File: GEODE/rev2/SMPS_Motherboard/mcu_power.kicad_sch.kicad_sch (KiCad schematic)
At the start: 32 parts, among them J402 Conn_Picoblade_JST_DEBUG, J403 USB4105-GF-A, U401 STM32G483RET6, Y401 ABM8W-48.0000MHZ-4-D1X-T3

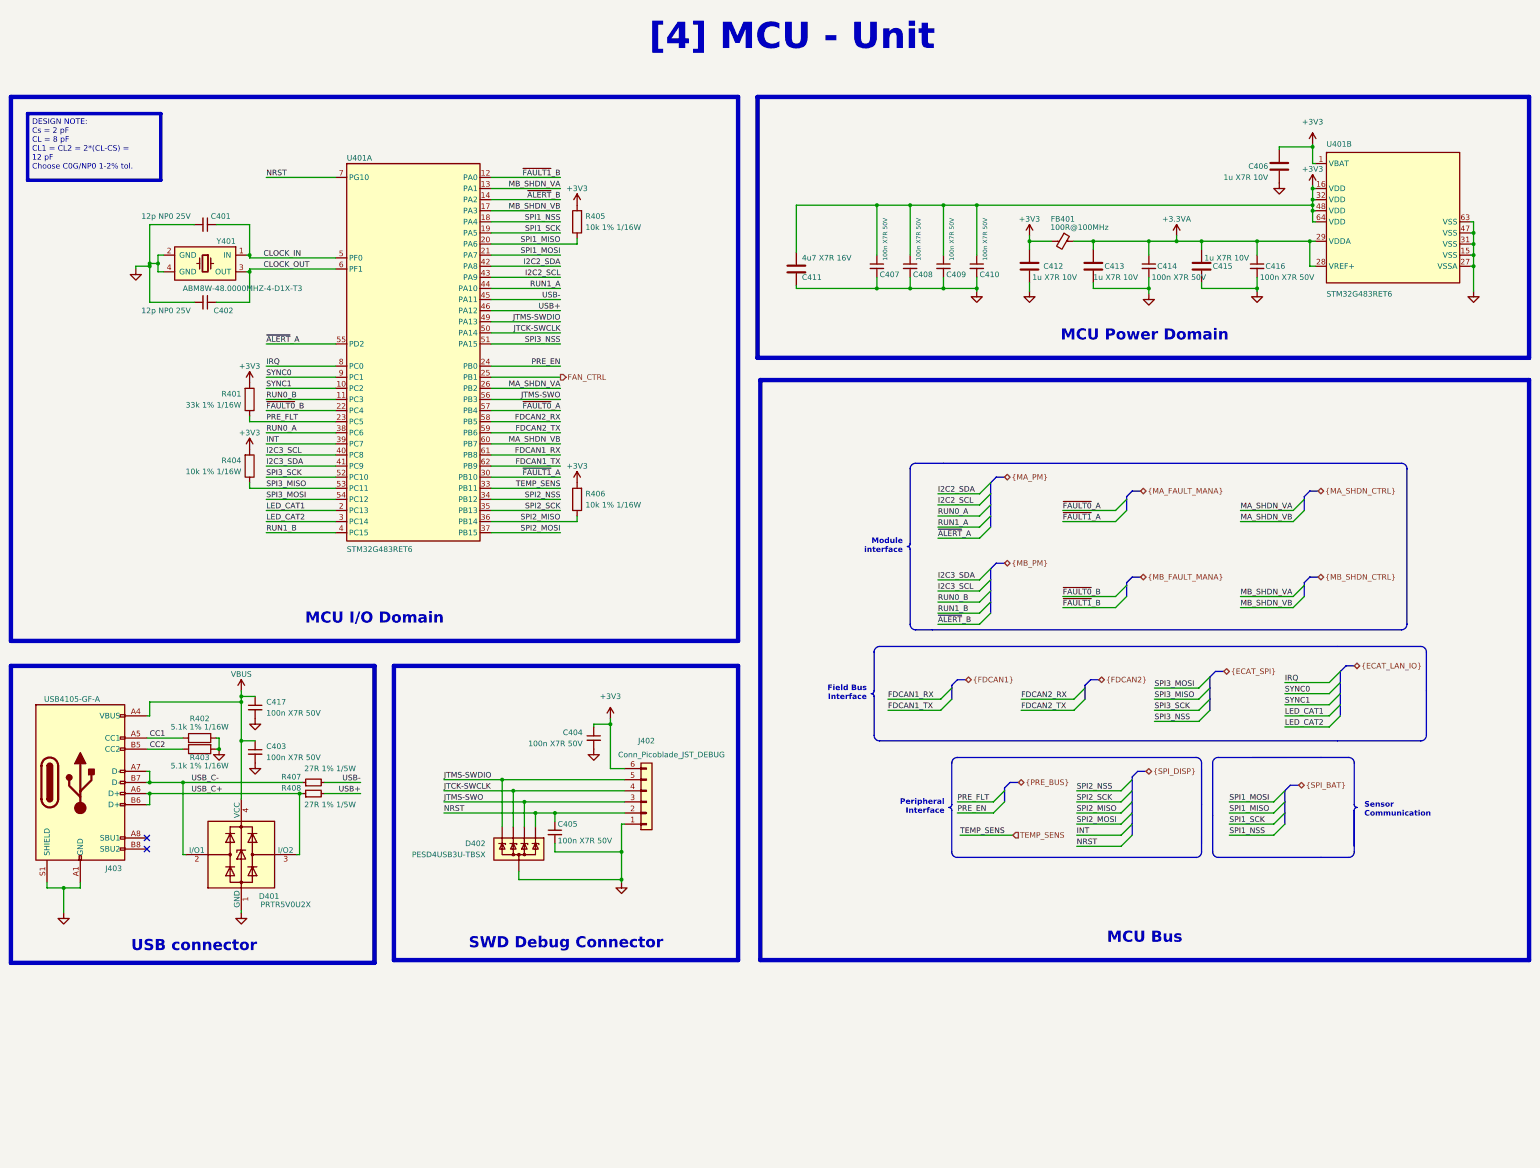
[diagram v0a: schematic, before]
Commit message: changed connectors, removed can, added fuse, disconnected EXTVCC in power generation
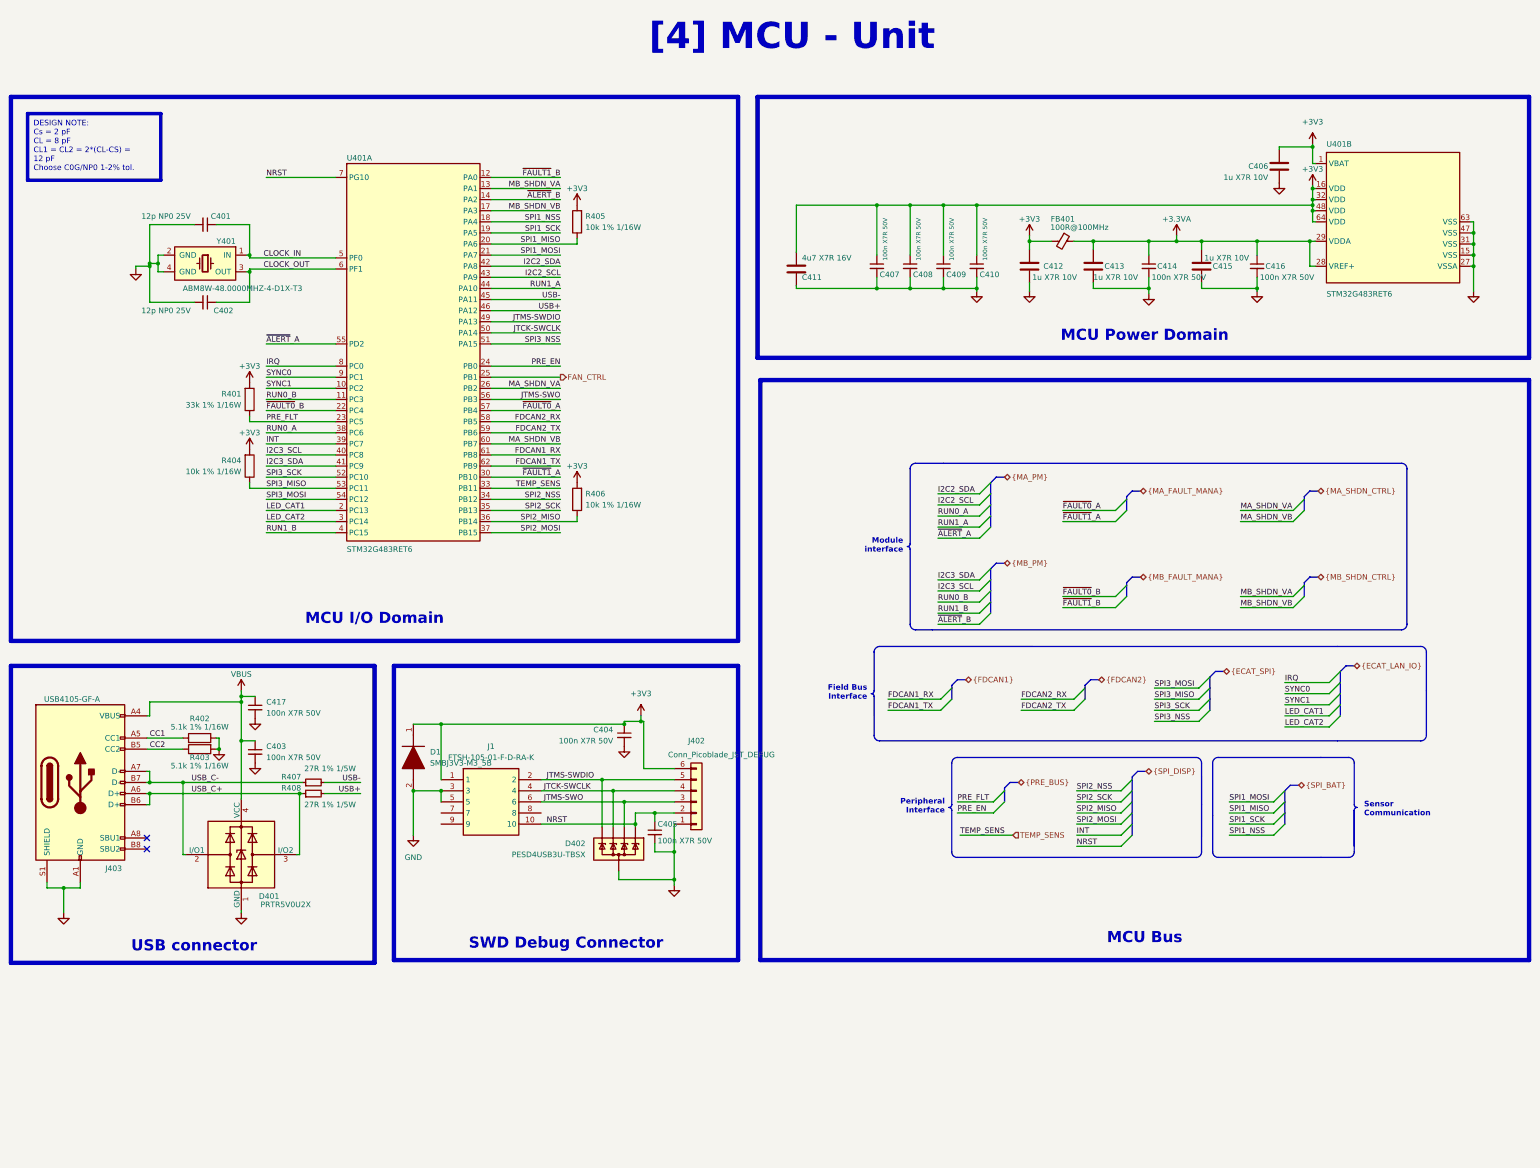
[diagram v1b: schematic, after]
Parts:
- added D1: SMBJ3V3-M3_5B, DIONM5436X244N, symbol SamacSys_Parts:SMBJ3V3-M3_5B
- added J1: FTSH-105-01-F-D-RA-K, FTSH-105-XX-YYY-D-RA-K, symbol SamacSys_Parts:FTSH-105-01-F-D-RA-K
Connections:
- net +3V3: now also D1.1 (K), J1.1
- net GND: now also D1.2 (A), J1.3, J1.5
- net JTCK-SWCLK: now also J1.4
- net JTMS-SWDIO: now also J1.2
- net JTMS-SWO: now also J1.6
- net NRST: now also J1.10
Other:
- moved on the sheet: C404, C405, D402, J402

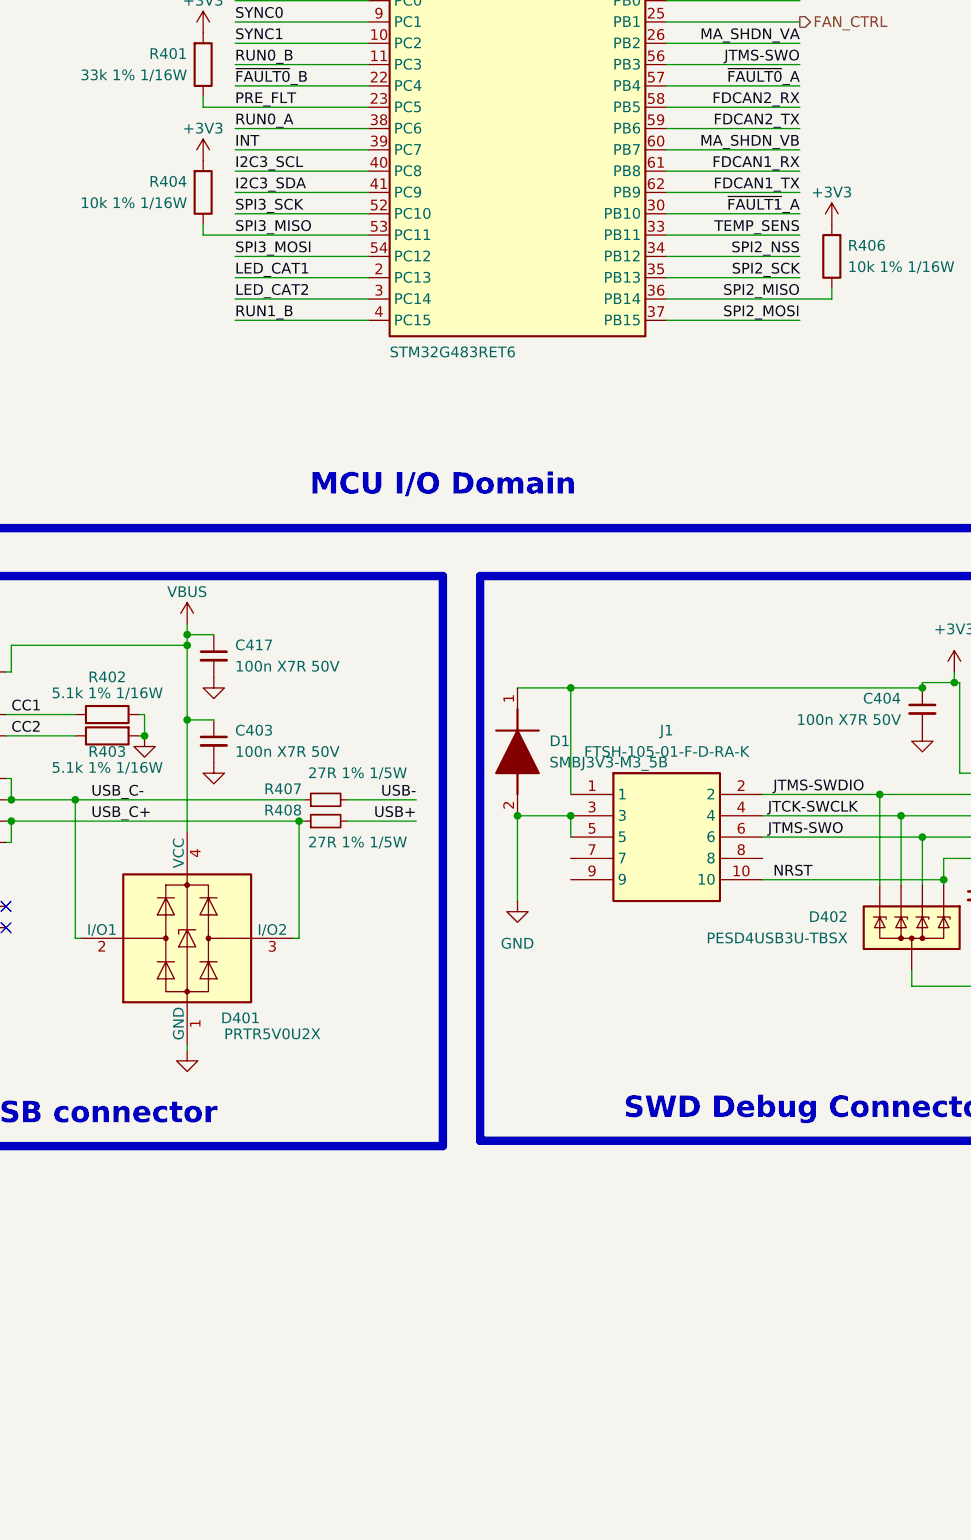
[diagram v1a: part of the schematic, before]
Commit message: replaced output connectors, added UART connector, removed fuse - schematics
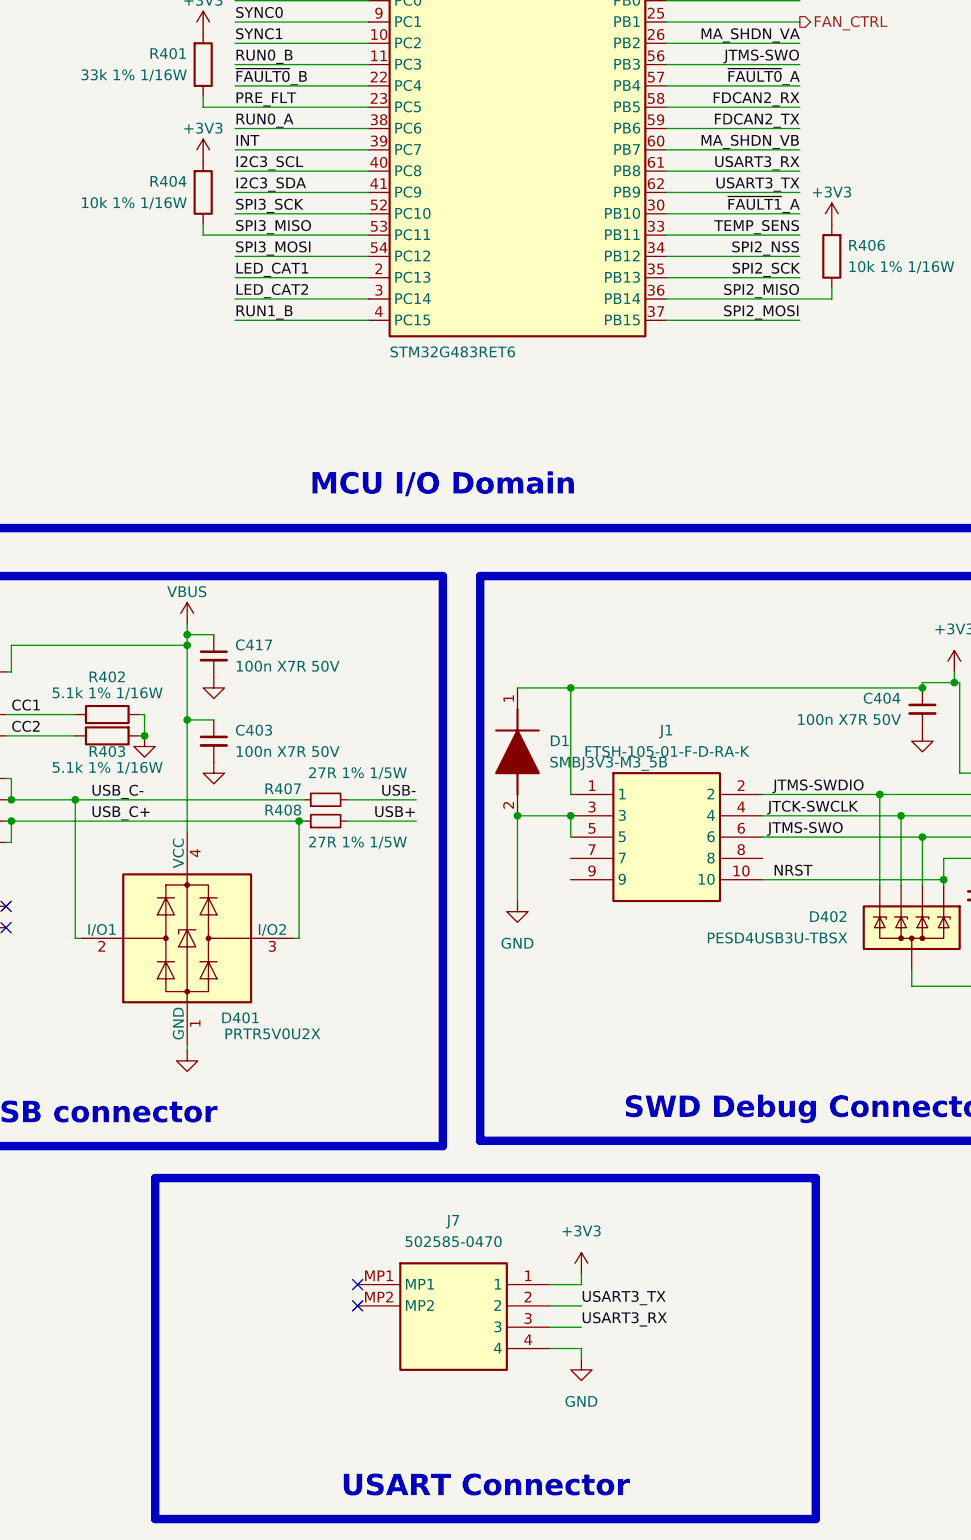
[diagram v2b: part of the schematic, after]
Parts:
- added J7: 502585-0470, 5025850470, symbol SamacSys_Parts:502585-0470
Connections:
- net +3V3: now also J7.1
- net FDCAN1_RX: no longer U401.61 (PB8)
- net FDCAN1_TX: no longer U401.62 (PB9)
- net GND: now also J7.4
- new net USART3_RX: J7.3, U401.61 (PB8)
- new net USART3_TX: J7.2, U401.62 (PB9)
- no-connect marks 2 -> 4
